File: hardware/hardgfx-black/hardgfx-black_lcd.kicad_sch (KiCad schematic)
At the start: 28 parts, among them J12 FH12-50S-0.5SH, J13 FH12-10S-0.5SH, J14 ~{LCD_RST}, J15 ~{LCD_WAKE}, J16 MODE, J17 LR, J18 UD, J19 DITH, U8 TPS61041DRVT

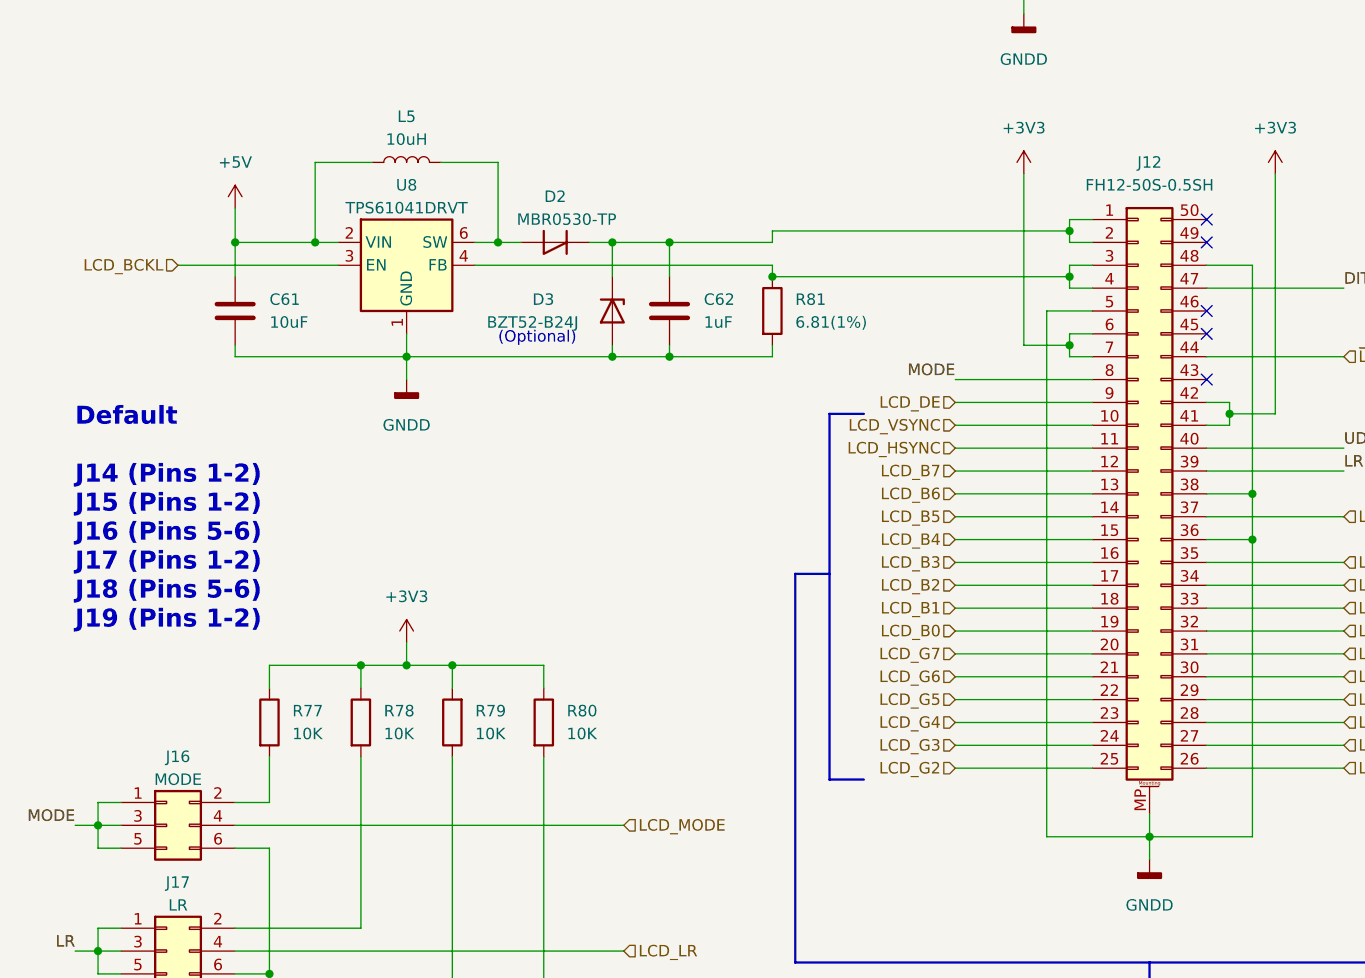
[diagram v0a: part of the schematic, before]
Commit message: Finish first schematic version.
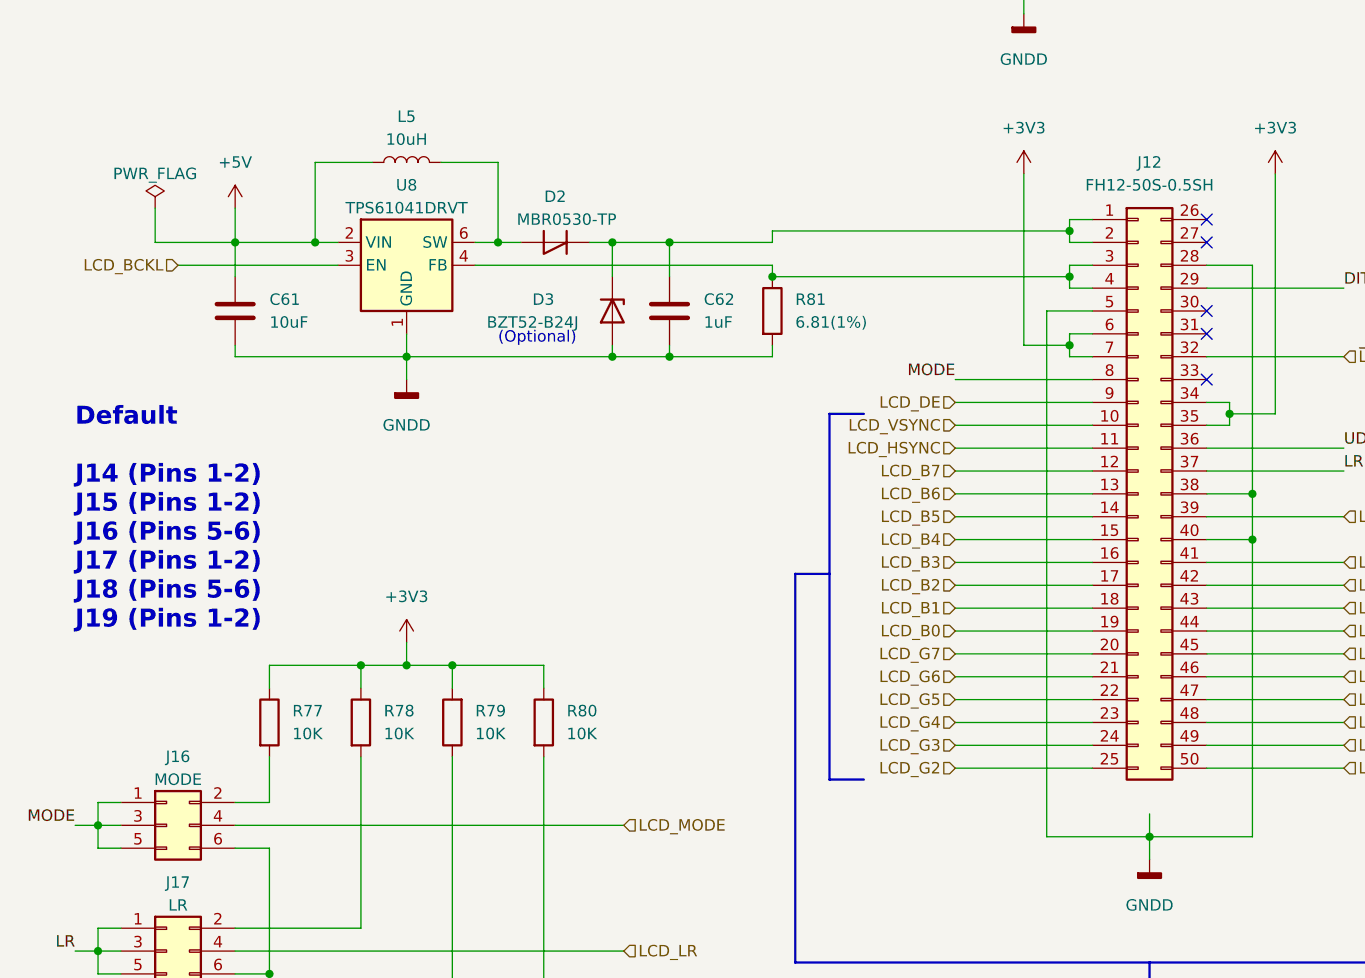
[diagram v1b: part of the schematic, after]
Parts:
- removed J12: FH12-50S-0.5SH, Connector_FFC-FPC:TE_5-1734839-0_1x50-1MP_P0.5mm_Horizontal, symbol Connector_Generic_MountingPin:Conn_02x25_Counter_Clockwise_MountingPin
- added J12: FH12-50S-0.5SH, Connector_FFC-FPC:TE_5-1734839-0_1x50-1MP_P0.5mm_Horizontal, symbol Connector_Generic:Conn_02x25_Top_Bottom
- J14, J15, J16, J17, J18, J19: MANUFACTURER Molex -> Samtec Inc.; digikey# 0702800631-ND -> SAM1028-03-ND; manf# 70280-0631 -> TSW-103-07-G-D; mouser# 538-70280-0631 -> 200-TSW10307GD
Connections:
- net +3V3: now also J12.34 (Pin_34), J12.35 (Pin_35), J12.6 (Pin_6), J12.7 (Pin_7)
- net DITH: now also J12.29 (Pin_29)
- net GNDD: now also J12.28 (Pin_28), J12.38 (Pin_38), J12.40 (Pin_40), J12.5 (Pin_5)
- net LCD_B0: now also J12.19 (Pin_19)
- net LCD_B1: now also J12.18 (Pin_18)
- net LCD_B2: now also J12.17 (Pin_17)
- net LCD_B3: now also J12.16 (Pin_16)
- net LCD_B4: now also J12.15 (Pin_15)
- net LCD_B5: now also J12.14 (Pin_14)
- net LCD_B6: now also J12.13 (Pin_13)
- net LCD_B7: now also J12.12 (Pin_12)
- net LCD_DCLK: now also J12.39 (Pin_39)
- net LCD_DE: now also J12.9 (Pin_9)
- net LCD_G0: now also J12.49 (Pin_49)
- net LCD_G1: now also J12.50 (Pin_50)
- net LCD_G2: now also J12.25 (Pin_25)
- net LCD_G3: now also J12.24 (Pin_24)
- net LCD_G4: now also J12.23 (Pin_23)
- net LCD_G5: now also J12.22 (Pin_22)
- net LCD_G6: now also J12.21 (Pin_21)
- net LCD_G7: now also J12.20 (Pin_20)
- net LCD_HSYNC: now also J12.11 (Pin_11)
- net LCD_R0: now also J12.41 (Pin_41)
- net LCD_R1: now also J12.42 (Pin_42)
- net LCD_R2: now also J12.43 (Pin_43)
- net LCD_R3: now also J12.44 (Pin_44)
- net LCD_R4: now also J12.45 (Pin_45)
- net LCD_R5: now also J12.46 (Pin_46)
- net LCD_R6: now also J12.47 (Pin_47)
- net LCD_R7: now also J12.48 (Pin_48)
- net LCD_VSYNC: now also J12.10 (Pin_10)
- net LR: now also J12.37 (Pin_37)
- net MODE: now also J12.8 (Pin_8)
- net UD: now also J12.36 (Pin_36)
- net ~{LCD_RST}: now also J12.32 (Pin_32)
- net at C62.1, D2.1 (K), D3.1 (K): now also J12.1 (Pin_1), J12.2 (Pin_2)
- net at R81.1, U8.4 (FB): now also J12.3 (Pin_3), J12.4 (Pin_4)

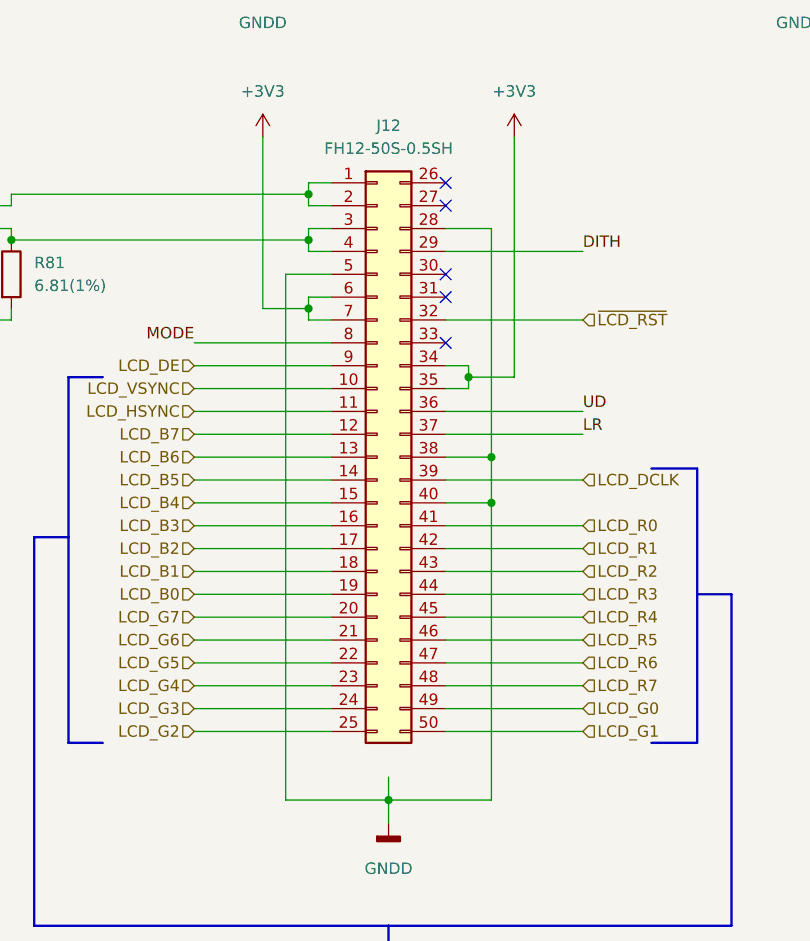
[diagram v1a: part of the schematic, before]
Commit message: J12 connector symbol and footprint modified. Previous J12 connector had incorrect connections.
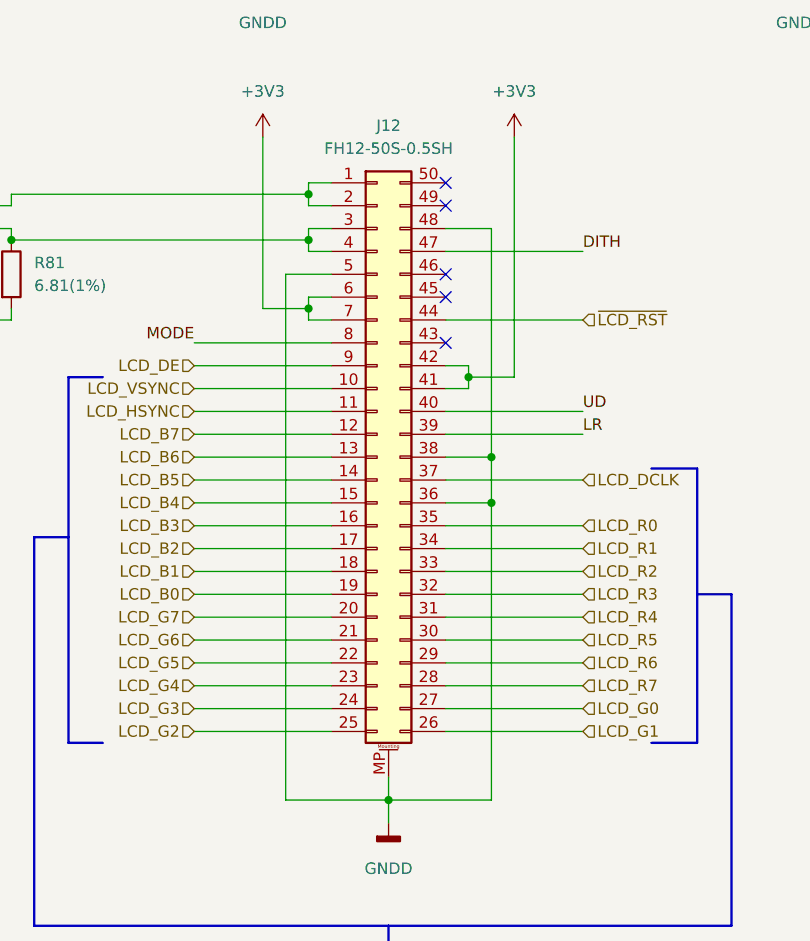
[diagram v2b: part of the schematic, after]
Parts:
- removed J12: FH12-50S-0.5SH, Connector_FFC-FPC:TE_5-1734839-0_1x50-1MP_P0.5mm_Horizontal, symbol Connector_Generic:Conn_02x25_Top_Bottom
- added J12: FH12-50S-0.5SH, Connector_FFC-FPC:TE_5-1734839-0_1x50-1MP_P0.5mm_Horizontal, symbol Connector_Generic_MountingPin:Conn_02x25_Counter_Clockwise_MountingPin
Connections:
- net +3V3: now also J12.41 (Pin_41), J12.42 (Pin_42), J12.6 (Pin_6), J12.7 (Pin_7)
- net DITH: now also J12.47 (Pin_47)
- net GNDD: now also J12.36 (Pin_36), J12.38 (Pin_38), J12.48 (Pin_48), J12.5 (Pin_5), J12.MP (MountPin)
- net LCD_B0: now also J12.19 (Pin_19)
- net LCD_B1: now also J12.18 (Pin_18)
- net LCD_B2: now also J12.17 (Pin_17)
- net LCD_B3: now also J12.16 (Pin_16)
- net LCD_B4: now also J12.15 (Pin_15)
- net LCD_B5: now also J12.14 (Pin_14)
- net LCD_B6: now also J12.13 (Pin_13)
- net LCD_B7: now also J12.12 (Pin_12)
- net LCD_DCLK: now also J12.37 (Pin_37)
- net LCD_DE: now also J12.9 (Pin_9)
- net LCD_G0: now also J12.27 (Pin_27)
- net LCD_G1: now also J12.26 (Pin_26)
- net LCD_G2: now also J12.25 (Pin_25)
- net LCD_G3: now also J12.24 (Pin_24)
- net LCD_G4: now also J12.23 (Pin_23)
- net LCD_G5: now also J12.22 (Pin_22)
- net LCD_G6: now also J12.21 (Pin_21)
- net LCD_G7: now also J12.20 (Pin_20)
- net LCD_HSYNC: now also J12.11 (Pin_11)
- net LCD_R0: now also J12.35 (Pin_35)
- net LCD_R1: now also J12.34 (Pin_34)
- net LCD_R2: now also J12.33 (Pin_33)
- net LCD_R3: now also J12.32 (Pin_32)
- net LCD_R4: now also J12.31 (Pin_31)
- net LCD_R5: now also J12.30 (Pin_30)
- net LCD_R6: now also J12.29 (Pin_29)
- net LCD_R7: now also J12.28 (Pin_28)
- net LCD_VSYNC: now also J12.10 (Pin_10)
- net LR: now also J12.39 (Pin_39)
- net MODE: now also J12.8 (Pin_8)
- net UD: now also J12.40 (Pin_40)
- net ~{LCD_RST}: now also J12.44 (Pin_44)
- net at C62.1, D2.1 (K), D3.1 (K): now also J12.1 (Pin_1), J12.2 (Pin_2)
- net at R81.1, U8.4 (FB): now also J12.3 (Pin_3), J12.4 (Pin_4)

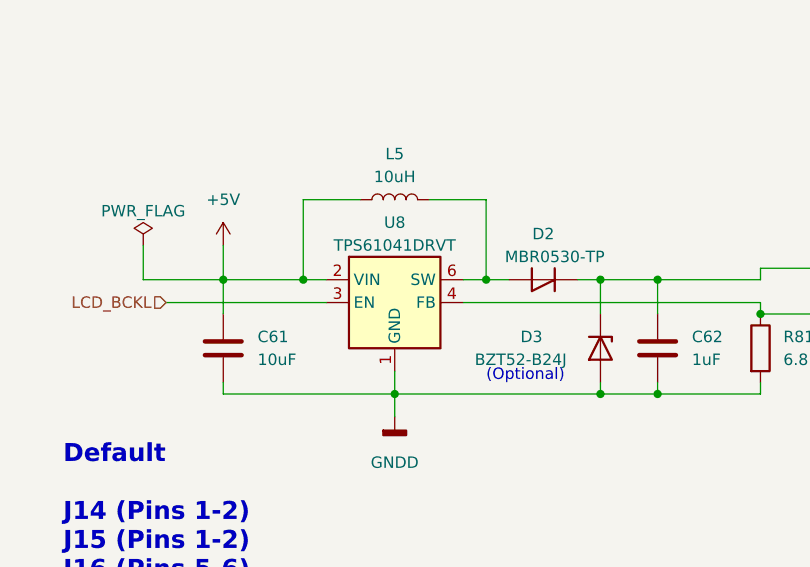
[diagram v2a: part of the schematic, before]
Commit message: Adding application note PDF document and change backlight controller.
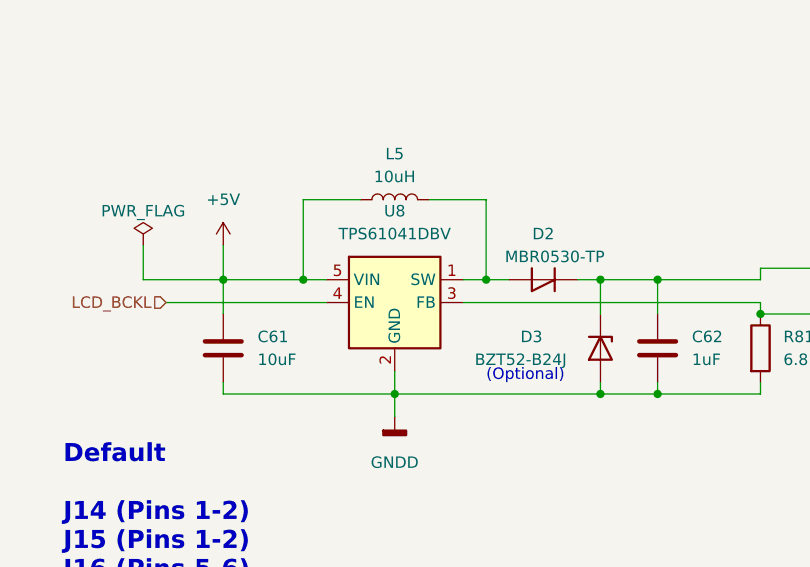
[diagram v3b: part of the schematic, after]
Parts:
- removed U8: TPS61041DRVT, Package_SON:WSON-6-1EP_2x2mm_P0.65mm_EP1x1.6mm, symbol Regulator_Switching:TPS61041DRV
- added U8: TPS61041DBV, Package_TO_SOT_SMD:SOT-23-5, symbol Regulator_Switching:TPS61041DBV
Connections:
- net +5V: now also U8.5 (VIN)
- net GNDD: now also U8.2 (GND)
- net LCD_BCKL: now also U8.4 (EN)
- net at D2.2 (A), L5.2: now also U8.1 (SW)
- net at J12.3 (Pin_3), J12.4 (Pin_4), R81.1: now also U8.3 (FB)
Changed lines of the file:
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@@
   (junction (at 151.13 107.95) (diameter 0) (color 0 0 0 0)
   )
+  (junction (at 97.79 78.74) (diameter 0) (color 0 0 0 0)
+  )
   (junction (at 274.32 66.04) (diameter 0) (color 0 0 0 0)
   )
@@
   (junction (at 22.86 139.7) (diameter 0) (color 0 0 0 0)
   )
-  (junction (at 97.79 78.74) (diameter 0) (color 0 0 0 0)
-  )
   (junction (at 266.7 58.42) (diameter 0) (color 0 0 0 0)
   )
@@
   (junction (at 125.73 34.29) (diameter 0) (color 0 0 0 0)
   )
+  (junction (at 67.31 74.93) (diameter 0) (color 0 0 0 0)
+  )
   (junction (at 224.79 45.72) (diameter 0) (color 0 0 0 0)
   )
@@
   (junction (at 38.1 74.93) (diameter 0) (color 0 0 0 0)
   )
-  (junction (at 67.31 74.93) (diameter 0) (color 0 0 0 0)
-  )
   (junction (at 237.49 77.47) (diameter 0) (color 0 0 0 0)
   )
@@
   (junction (at 52.07 121.92) (diameter 0) (color 0 0 0 0)
   )
+  (junction (at 46.99 74.93) (diameter 0) (color 0 0 0 0)
+  )
   (junction (at 57.15 87.63) (diameter 0) (color 0 0 0 0)
-  )
-  (junction (at 46.99 74.93) (diameter 0) (color 0 0 0 0)
   )
   (junction (at 41.91 156.21) (diameter 0) (color 0 0 0 0)
@@
     (stroke (width 0) (type default) (color 0 0 0 0))
   )
-  (wire (pts (xy 97.79 77.47) (xy 97.79 78.74))
-    (stroke (width 0) (type default) (color 0 0 0 0))
-  )
   (wire (pts (xy 67.31 74.93) (xy 69.85 74.93))
     (stroke (width 0) (type default) (color 0 0 0 0))
@@
     (stroke (width 0) (type default) (color 0 0 0 0))
   )
-  (wire (pts (xy 31.75 77.47) (xy 49.53 77.47))
-    (stroke (width 0) (type default) (color 0 0 0 0))
-  )
   (wire (pts (xy 38.1 153.67) (xy 81.28 153.67))
-    (stroke (width 0) (type default) (color 0 0 0 0))
-  )
-  (wire (pts (xy 67.31 74.93) (xy 64.77 74.93))
     (stroke (width 0) (type default) (color 0 0 0 0))
   )
@@
     (stroke (width 0.254) (type default) (color 0 0 0 0))
   )
+  (wire (pts (xy 220.98 74.93) (xy 214.63 74.93))
+    (stroke (width 0) (type default) (color 0 0 0 0))
+  )
+  (wire (pts (xy 214.63 62.23) (xy 214.63 64.77))
+    (stroke (width 0) (type default) (color 0 0 0 0))
+  )
+  (wire (pts (xy 38.1 87.63) (xy 57.15 87.63))
+    (stroke (width 0) (type default) (color 0 0 0 0))
+  )
   (wire (pts (xy 57.15 85.09) (xy 57.15 87.63))
     (stroke (width 0) (type default) (color 0 0 0 0))
   )
-  (wire (pts (xy 220.98 74.93) (xy 214.63 74.93))
-    (stroke (width 0) (type default) (color 0 0 0 0))
-  )
-  (wire (pts (xy 214.63 62.23) (xy 214.63 64.77))
-    (stroke (width 0) (type default) (color 0 0 0 0))
-  )
-  (wire (pts (xy 38.1 87.63) (xy 57.15 87.63))
-    (stroke (width 0) (type default) (color 0 0 0 0))
-  )
   (wire (pts (xy 25.4 156.21) (xy 22.86 156.21))
     (stroke (width 0) (type default) (color 0 0 0 0))
   )
+  (wire (pts (xy 64.77 74.93) (xy 67.31 74.93))
+    (stroke (width 0) (type default) (color 0 0 0 0))
+  )
   (wire (pts (xy 214.63 115.57) (xy 214.63 113.03))
     (stroke (width 0) (type default) (color 0 0 0 0))
@@
   )
   (wire (pts (xy 214.63 40.64) (xy 269.24 40.64))
-    (stroke (width 0) (type default) (color 0 0 0 0))
-  )
-  (wire (pts (xy 46.99 74.93) (xy 49.53 74.93))
     (stroke (width 0) (type default) (color 0 0 0 0))
   )
@@
     (stroke (width 0) (type default) (color 0 0 0 0))
   )
+  (wire (pts (xy 64.77 77.47) (xy 97.79 77.47))
+    (stroke (width 0) (type default) (color 0 0 0 0))
+  )
   (wire (pts (xy 60.96 66.04) (xy 67.31 66.04))
     (stroke (width 0) (type default) (color 0 0 0 0))
@@
     (stroke (width 0) (type default) (color 0 0 0 0))
   )
+  (wire (pts (xy 31.75 77.47) (xy 49.53 77.47))
+    (stroke (width 0) (type default) (color 0 0 0 0))
+  )
   (wire (pts (xy 38.1 179.07) (xy 72.39 179.07))
     (stroke (width 0) (type default) (color 0 0 0 0))
@@
   )
   (wire (pts (xy 148.59 92.71) (xy 148.59 93.98))
+    (stroke (width 0) (type default) (color 0 0 0 0))
+  )
+  (wire (pts (xy 97.79 77.47) (xy 97.79 78.74))
     (stroke (width 0) (type default) (color 0 0 0 0))
   )
@@
     (stroke (width 0) (type default) (color 0 0 0 0))
   )
+  (wire (pts (xy 46.99 74.93) (xy 49.53 74.93))
+    (stroke (width 0) (type default) (color 0 0 0 0))
+  )
   (wire (pts (xy 146.05 80.01) (xy 161.29 80.01))
     (stroke (width 0) (type default) (color 0 0 0 0))
@@
   )
   (wire (pts (xy 22.86 151.13) (xy 22.86 153.67))
-    (stroke (width 0) (type default) (color 0 0 0 0))
-  )
-  (wire (pts (xy 64.77 77.47) (xy 97.79 77.47))
     (stroke (width 0) (type default) (color 0 0 0 0))
   )
@@
     (pin "1")
   )
+  (symbol (lib_id "Regulator_Switching:TPS61041DBV") (at 57.15 77.47 0) (unit 1)
+    (in_bom yes) (on_board yes) (fields_autoplaced)
+    (property "Reference" "U8" (id 0) (at 57.15 67.31 0))
+    (property "Value" "TPS61041DBV" (id 1) (at 57.15 69.85 0))
+    (property "Footprint" "Package_TO_SOT_SMD:SOT-23-5" (id 2) (at 59.69 83.82 0)
+      (effects (font (size 1.27 1.27) italic) (justify left) hide)
+    )
+    (property "Datasheet" "https://www.ti.com/lit/ds/symlink/tps61040.pdf?HQS=dis-dk-null-digikeymode-dsf-pf-null-wwe&ts=1672455472321&ref_url=https%253A%252F%252Fwww.ti.com%252Fgeneral%252Fdocs%252Fsuppproductinfo.tsp%253FdistId%253D10%2526gotoUrl%253Dhttps%253A%252F%252Fwww.ti.com%252Flit%252Fgpn%252Ftps61040" (id 3) (at 52.07 69.85 0)
+      (effects (font (size 1.27 1.27)) hide)
+    )
+    (property "MANUFACTURER" "Texas Instruments" (id 4) (at 57.15 77.47 0)
+      (effects (font (size 1.27 1.27)) hide)
+    )
+    (property "digikey#" "296-12686-1-ND" (id 5) (at 57.15 77.47 0)
+      (effects (font (size 1.27 1.27)) hide)
+    )
+    (property "manf#" "TPS61041DBVR" (id 6) (at 57.15 77.47 0)
+      (effects (font (size 1.27 1.27)) hide)
+    )
+    (property "mouser#" "595-TPS61041DBVR" (id 7) (at 57.15 77.47 0)
+      (effects (font (size 1.27 1.27)) hide)
+    )
+    (pin "1")
+    (pin "2")
+    (pin "3")
+    (pin "4")
+    (pin "5")
+  )
   (symbol (lib_id "power:+3V3") (at 153.67 67.31 0) (unit 1)
     (in_bom yes) (on_board yes) (fields_autoplaced)
@@
     (pin "2")
   )
-  (symbol (lib_id "Regulator_Switching:TPS61041DRV") (at 57.15 77.47 0) (unit 1)
-    (in_bom yes) (on_board yes)
-    (property "Reference" "U8" (id 0) (at 57.15 68.58 0))
-    (property "Value" "TPS61041DRVT" (id 1) (at 57.15 71.12 0))
-    (property "Footprint" "Package_SON:WSON-6-1EP_2x2mm_P0.65mm_EP1x1.6mm" (id 2) (at 58.42 83.82 0)
-      (effects (font (size 1.27 1.27) italic) (justify left) hide)
-    )
-    (property "Datasheet" "http://www.ti.com/lit/ds/symlink/tps61040.pdf" (id 3) (at 60.96 68.58 0)
-      (effects (font (size 1.27 1.27)) hide)
-    )
-    (property "MANUFACTURER" "Texas Instruments" (id 4) (at 57.15 77.47 0)
-      (effects (font (size 1.27 1.27)) hide)
-    )
-    (property "manf#" "TPS61041DRVT" (id 5) (at 57.15 77.47 0)
-      (effects (font (size 1.27 1.27)) hide)
-    )
-    (property "digikey#" "296-41851-1-ND" (id 6) (at 57.15 77.47 0)
-      (effects (font (size 1.27 1.27)) hide)
-    )
-    (property "mouser#" "595-TPS61041DRVT" (id 7) (at 57.15 77.47 0)
-      (effects (font (size 1.27 1.27)) hide)
-    )
-    (pin "1")
-    (pin "2")
-    (pin "3")
-    (pin "4")
-    (pin "5")
-    (pin "6")
-  )
   (symbol (lib_id "Connector_Generic:Conn_02x03_Odd_Even") (at 226.06 77.47 0) (unit 1)
